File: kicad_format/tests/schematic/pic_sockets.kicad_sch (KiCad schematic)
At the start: 7 parts, among them P2 SUPP28, P3 SUPP40, U1 24Cxx, U5 PIC_18_PINS, U6 PIC_8_PINS

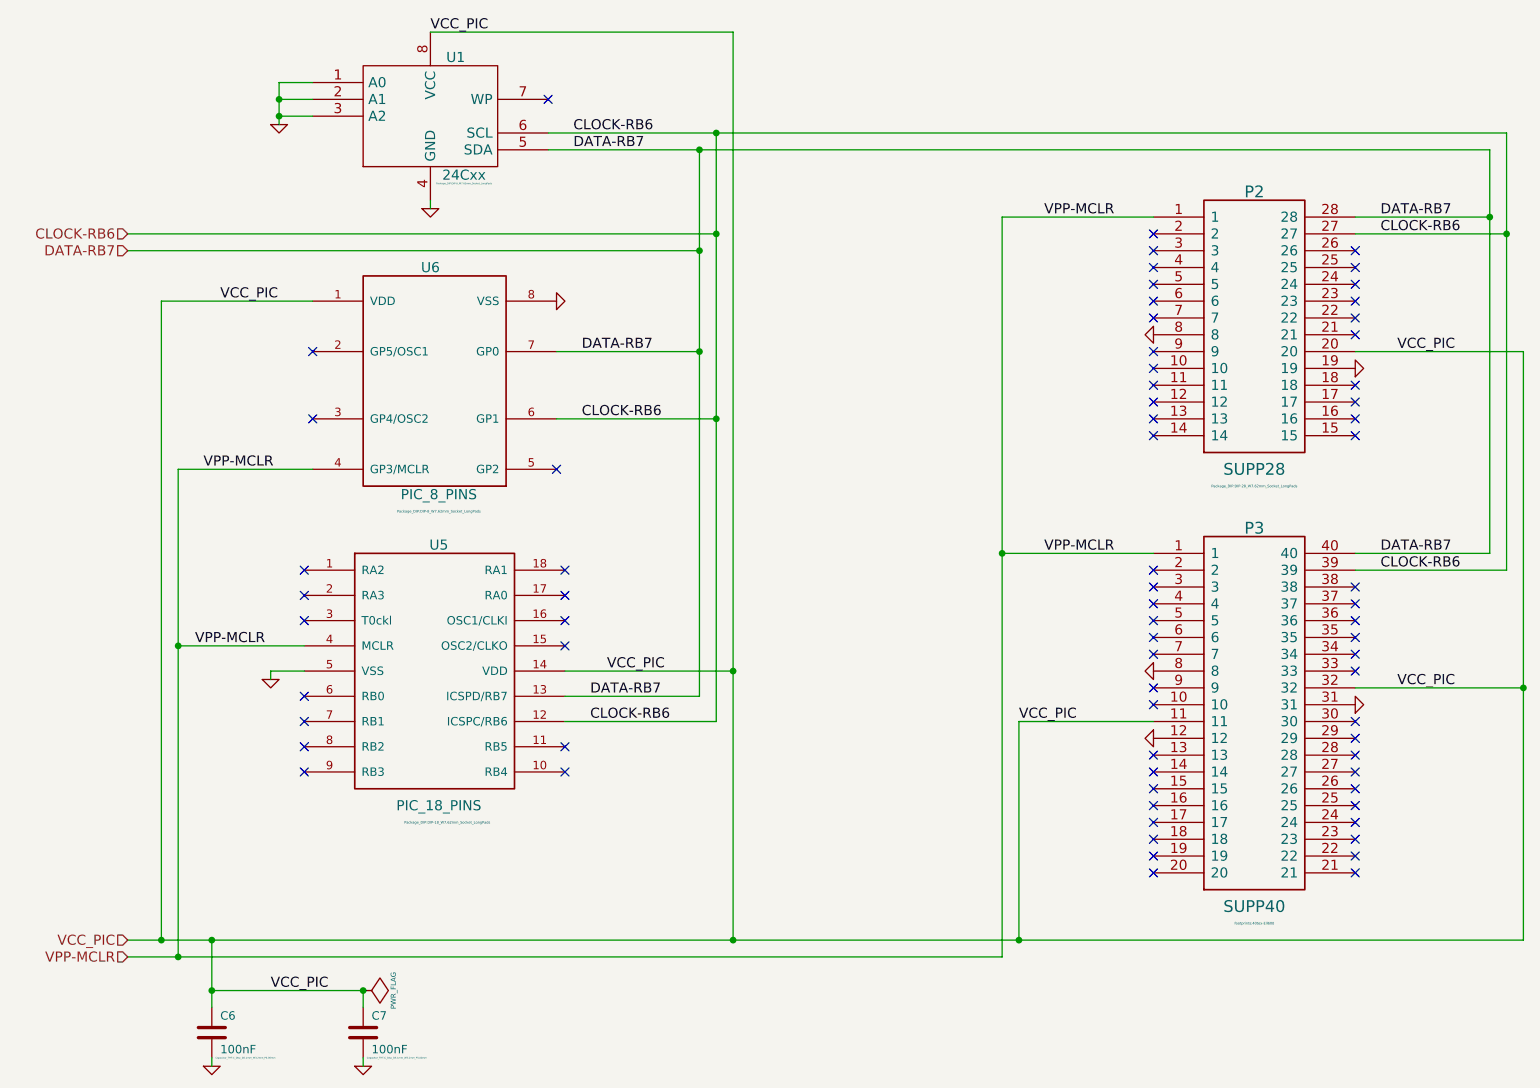
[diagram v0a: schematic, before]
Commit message: Add serialization context and support most modern kicad file idiosyncrasies
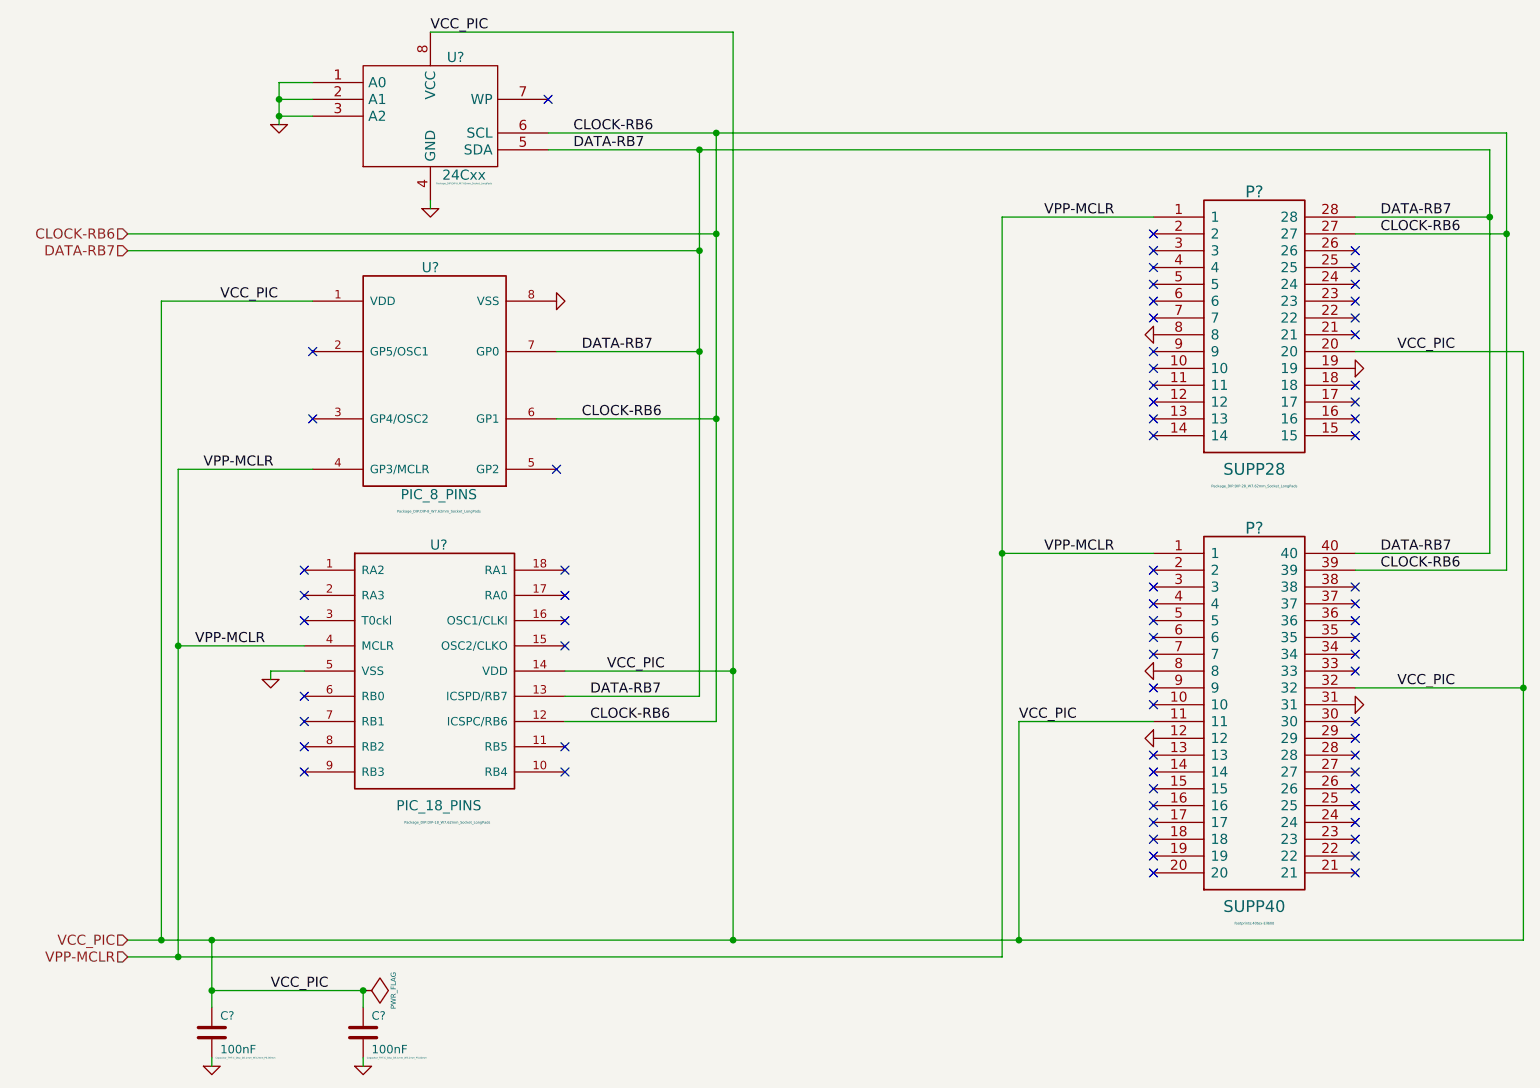
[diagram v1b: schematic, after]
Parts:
- renumbered C6 to C?, C7 to C?, P3 to P?, P2 to P?, U6 to U?, U5 to U?, U1 to U?
